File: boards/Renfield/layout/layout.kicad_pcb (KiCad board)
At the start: 4 copper layers, 74 x 52 mm, 99 parts, among them IC1 DS04-254-1-04BK-SMT, IC2 TPD4E05U06QDQARQ1, J1 2060-452/998-404, J2 61000821121, J3 ?, J4 61000418221, J5 USB4105-GF-A, Q1 CSD13380F3, Q2 CSD17318Q2, SW1 B3U-1000P, SW2 B3U-1000P, U1 TPSM33606S5QRDNRQ1, U2 TPS259482LYWPR, U3 TPS74501PDRVR, U4 STM32G0B1KEU6N, U5 TCPP01-M12

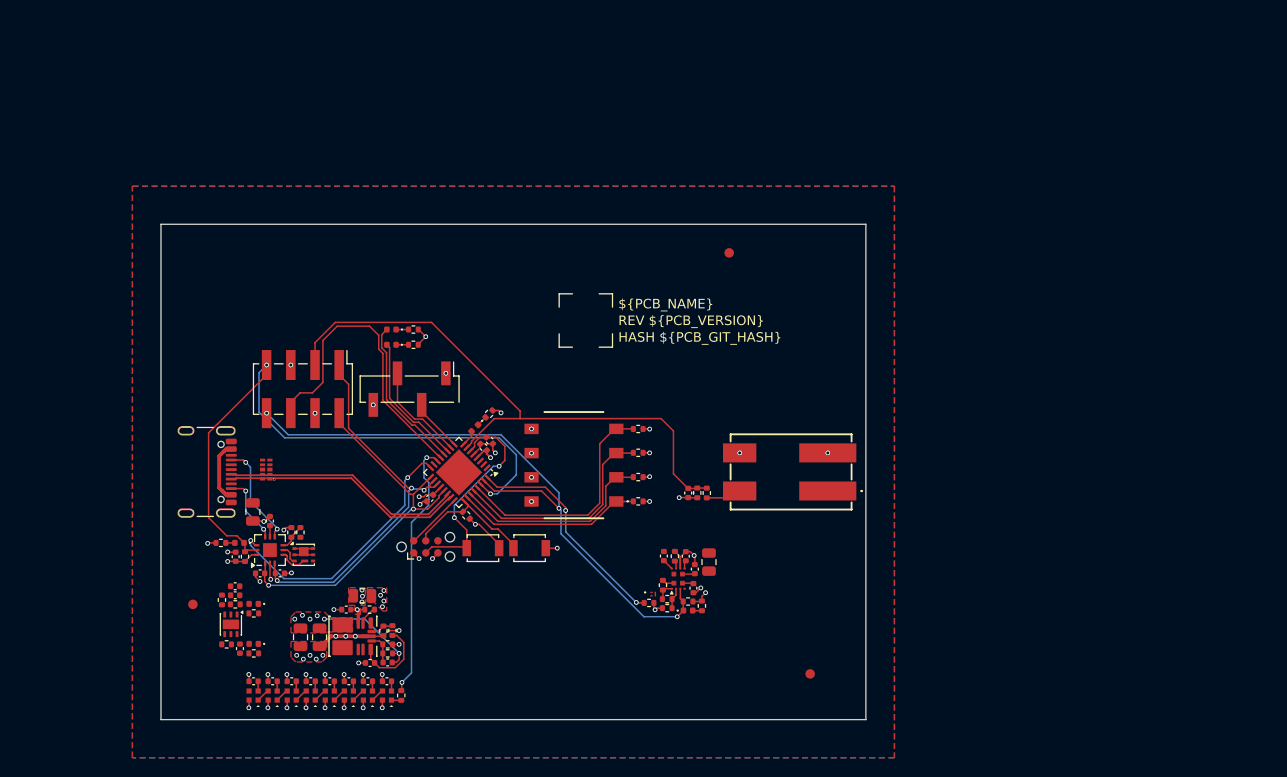
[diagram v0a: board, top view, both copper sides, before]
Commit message: refactor(Renfield): strip to minimal PD sink dev board
Simplified Renfield down to the essentials needed for STM32G0B1 UCPD
firmware development. Roughly halves the BOM and resolves a real
bootstrap bug in the rail topology.

Architectural fix: buck now sits on VBUS_RAW, not VBUS_PROT.
  Before: VBUS_RAW \u2192 FET \u2192 VBUS_PROT \u2192 Buck \u2192 V3V3 \u2192 TCPP01 VCC
          \u2191 but FET needs VCC to close (DS12900 conditions all VGS
          specs on VCC = 3.0\u20133.6 V). Circular; board couldn't boot.
  After:  VBUS_RAW \u2500\u252c\u2500\u2500 Buck \u2192 V3V3 \u2192 MCU + TCPP01 VCC
                  \u2514\u2500\u2500 FET  \u2192 VBUS_PROT \u2192 WAGO
          MCU boots off the receptacle directly; FET gates only the
          LOAD rail. MCU survives OVP trips. Matches DS12900 \u00a76.1:
          "separate the low voltage MCU domain from the high-voltage
          power path."

Removed (dev-board features not needed for PD firmware work):
  - TPS259482L eFuse + CSD13380F3 disable shunt + SPLYGD LED +
    VBUS_OUT bulk + VBUS_OUT ADC divider
  - 8x IN-PI15 WS2812 V-bargraph + series R
  - 4-pos DIP switch + 4x pull-up resistors
  - BOOT0 + RESET tactile buttons
  - 2x4 PD-dev probe header + 1x4 UART header
  - TPD4E05U06 USB-data ESD array
  - TPS74501P LDO (buck now goes VBUS_RAW \u2192 3.3 V directly with
    the TPSM33606S3 fixed-trim variant)
  - 5 V rail (nothing consumed it)
  - 5V_RAIL LED, EFUSE_NOT_GOOD LED

Kept (everything firmware dev actually needs):
  - USB-C 16P receptacle + TCPP01-M12 + CSD17318Q2 gated FET
  - TPSM33606S3 buck \u2192 V3V3
  - STM32G0B1KEU6N with UCPD1 / USB FS / SWD / UART
  - WAGO 2060-452 load output (post-FET)
  - Tag-Connect SWD pads
  - 5 status LEDs: 3V3_RAIL, TCPP01_FLT, heartbeat, PD contract, USB enum
  - 12x round \u00d81.0 mm SMD test pads (VBUS_RAW, VBUS_PROT, FET_GATE,
    V3V3, UART_TX, UART_RX, CC1, CC2, SCOPE_MARKER, TCPP01_FLT, 2x GND)

Other cleanup:
  - Dropped C_VBUS_RAW \u2014 TCPP01 internal C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
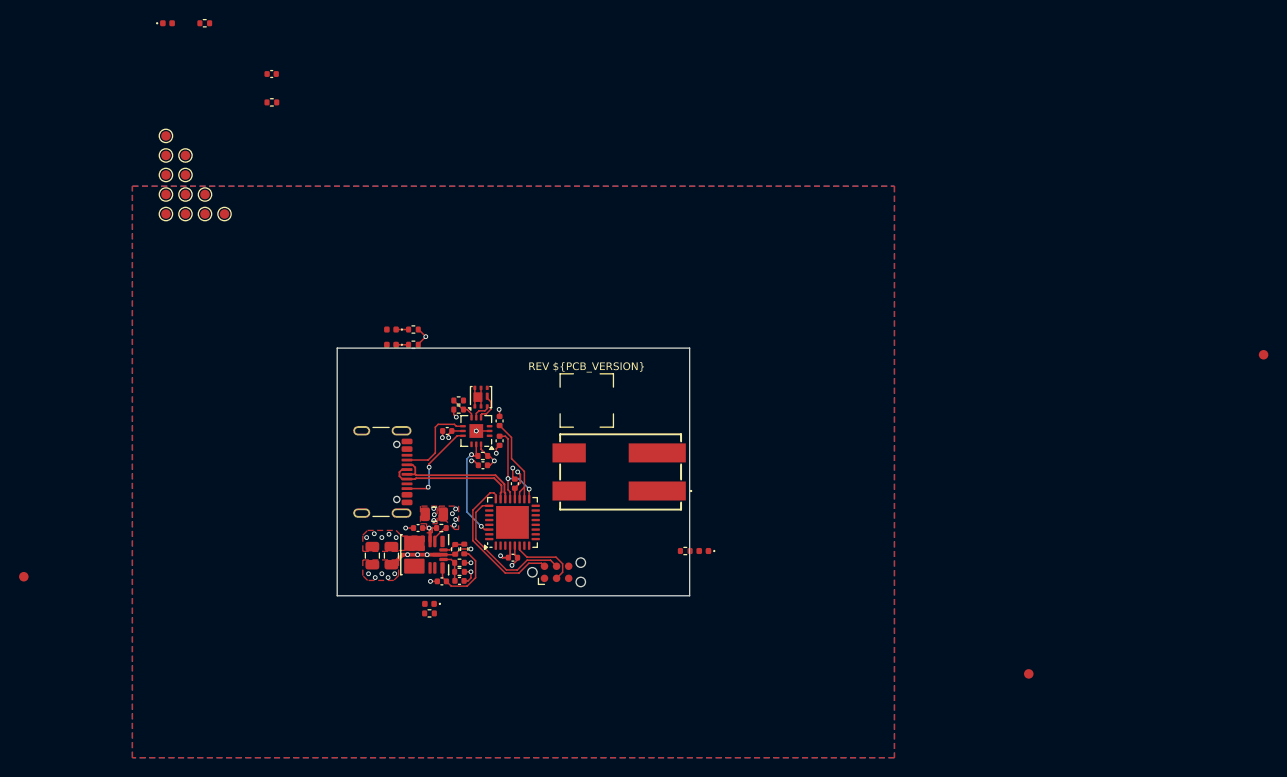
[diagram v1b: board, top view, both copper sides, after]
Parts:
- removed the C12 at (126.7, 122.0)
- removed the C13 at (124.7, 122.0)
- removed C14, C20, C26, C27, C28, C29: GRM155Z71A105KE01D, kicad_libraries_kicad-footprints_Capacitor_SMD@9.0.3:C_0402_1005Metric
- removed C15: GCM1555C1H100FA16D, kicad_libraries_kicad-footprints_Capacitor_SMD@9.0.3:C_0402_1005Metric
- removed C16: GRM21BZ71H475KE15K, kicad_libraries_kicad-footprints_Capacitor_SMD@9.0.3:C_0805_2012Metric
- removed C17, C22, C24: GCM155R71H104KE02D, kicad_libraries_kicad-footprints_Capacitor_SMD@9.0.3:C_0402_1005Metric
- removed C18, C19: GRM21BZ71A226ME15K, kicad_libraries_kicad-footprints_Capacitor_SMD@9.0.3:C_0805_2012Metric
- removed C21: GCM1555C1H102FA16D, kicad_libraries_kicad-footprints_Capacitor_SMD@9.0.3:C_0402_1005Metric
- removed C23, C25: GRM1555CYA103GE01D, kicad_libraries_kicad-footprints_Capacitor_SMD@9.0.3:C_0402_1005Metric
- removed D10, D6, D7, D8, D9: IN-PI15TAT5R5G5B, diodeinc_registry_components_Inolux_IN-PI15TAT5R5G5B@0.1.1:IN-PI15TAT5R5G5B
- removed D11: VLMS1500-GS08, kicad_libraries_kicad-footprints_LED_SMD@9.0.3:LED_0402_1005Metric
- removed D12: LTST-C281KSKT, kicad_libraries_kicad-footprints_LED_SMD@9.0.3:LED_0402_1005Metric
- removed the D3 at (136.7, 123.5)
- removed the D4 at (134.7, 123.5)
- removed the D5 at (132.7, 123.5)
- removed IC1: DS04-254-1-04BK-SMT, diodeinc_registry_components_DS04-254-1-04BK-SMT@0.3.7:DS04254104BKSMT
- removed IC2: TPD4E05U06QDQARQ1, diodeinc_registry_components_TPD4E05U06QDQARQ1@0.4.5:DQA_R-PUSON-N10_
- removed the J2 at (127.9, 91.3)
- removed J4: 61000418221, kicad_libraries_kicad-footprints_Connector_PinHeader_2.54mm@9.0.3:PinHeader_1x04_P2.54mm_Vertical_SMD_Pin1Left
- removed the Q1 at (164.7, 112.8)
- removed the R12 at (168.3, 113.6)
- removed R15: ERJ-2RKF9092X, kicad_libraries_kicad-footprints_Resistor_SMD@9.0.3:R_0402_1005Metric
- removed R16, R19: ERJ-2RKF1002X, kicad_libraries_kicad-footprints_Resistor_SMD@9.0.3:R_0402_1005Metric
- removed R17: ERJ-2RKF4700X, kicad_libraries_kicad-footprints_Resistor_SMD@9.0.3:R_0402_1005Metric
- removed R18, R21, R22, R27: ERJ-2RKF1003X, kicad_libraries_kicad-footprints_Resistor_SMD@9.0.3:R_0402_1005Metric
- removed R20: ERJ-2GE0R00X, kicad_libraries_kicad-footprints_Resistor_SMD@9.0.3:R_0402_1005Metric
- removed R23: ERJ-2RKF3653X, kicad_libraries_kicad-footprints_Resistor_SMD@9.0.3:R_0402_1005Metric
- removed R24: ERJ-2RKF2672X, kicad_libraries_kicad-footprints_Resistor_SMD@9.0.3:R_0402_1005Metric
- removed R25: ERJ-2RKF1053X, kicad_libraries_kicad-footprints_Resistor_SMD@9.0.3:R_0402_1005Metric
- removed R26: ERJ-2RKF8060X, kicad_libraries_kicad-footprints_Resistor_SMD@9.0.3:R_0402_1005Metric
- removed R28: ERJ-2RKF5102X, kicad_libraries_kicad-footprints_Resistor_SMD@9.0.3:R_0402_1005Metric
- removed R29: ERJ-2RKF2553X, kicad_libraries_kicad-footprints_Resistor_SMD@9.0.3:R_0402_1005Metric
- removed the R4 at (163.1, 103.1)
- removed the R5 at (163.1, 100.5)
- removed the R6 at (163.1, 98.0)
- removed SW1, SW2: B3U-1000P, diodeinc_registry_components_B3U-1000P@0.2.1:B3U-1000P
- removed the U3 at (120.3, 116.0)
- removed U4: STM32G0B1KEU6N, diodeinc_registry_components_STMicroelectronics_STM32G0B1KxUxN@0.1.4:QFN-32-1EP_5x5mm_P0.5mm_EP3.45x3.45mm
- added R11: ERJ-2RKF1003X, kicad_libraries_kicad-footprints_Resistor_SMD@9.0.3:R_0402_1005Metric, F.Cu at (144.8, 108.1)
- added TP1: ?, kicad_libraries_kicad-footprints_TestPoint@9.0.3:TestPoint_Pad_D1.0mm, F.Cu at (113.5, 72.9)
- added TP10: ?, kicad_libraries_kicad-footprints_TestPoint@9.0.3:TestPoint_Pad_D1.0mm, F.Cu at (119.7, 72.9)
- added TP11: ?, kicad_libraries_kicad-footprints_TestPoint@9.0.3:TestPoint_Pad_D1.0mm, F.Cu at (113.5, 64.7)
- added TP12: ?, kicad_libraries_kicad-footprints_TestPoint@9.0.3:TestPoint_Pad_D1.0mm, F.Cu at (115.6, 66.8)
- added TP2: ?, kicad_libraries_kicad-footprints_TestPoint@9.0.3:TestPoint_Pad_D1.0mm, F.Cu at (113.5, 70.9)
- added TP3: ?, kicad_libraries_kicad-footprints_TestPoint@9.0.3:TestPoint_Pad_D1.0mm, F.Cu at (115.6, 72.9)
- added TP4: ?, kicad_libraries_kicad-footprints_TestPoint@9.0.3:TestPoint_Pad_D1.0mm, F.Cu at (113.5, 68.8)
- added TP5: ?, kicad_libraries_kicad-footprints_TestPoint@9.0.3:TestPoint_Pad_D1.0mm, F.Cu at (115.6, 70.9)
- added TP6: ?, kicad_libraries_kicad-footprints_TestPoint@9.0.3:TestPoint_Pad_D1.0mm, F.Cu at (117.6, 72.9)
- added TP7: ?, kicad_libraries_kicad-footprints_TestPoint@9.0.3:TestPoint_Pad_D1.0mm, F.Cu at (113.5, 66.8)
- added TP8: ?, kicad_libraries_kicad-footprints_TestPoint@9.0.3:TestPoint_Pad_D1.0mm, F.Cu at (115.6, 68.8)
- added TP9: ?, kicad_libraries_kicad-footprints_TestPoint@9.0.3:TestPoint_Pad_D1.0mm, F.Cu at (117.6, 70.9)
- C4: value GRM21BZ71H475KE15K -> GCM1555C1H100FA16D; footprint kicad_libraries_kicad-footprints_Capacitor_SMD@9.0.3:C_0805_2012Metric -> kicad_libraries_kicad-footprints_Capacitor_SMD@9.0.3:C_0402_1005Metric
- C6: value GRM1555CYA103GE01D -> GCM155R71H104KE02D
- C7, C8: value GRM155Z71A105KE01D -> GRM21BZ71A226ME15K; footprint kicad_libraries_kicad-footprints_Capacitor_SMD@9.0.3:C_0402_1005Metric -> kicad_libraries_kicad-footprints_Capacitor_SMD@9.0.3:C_0805_2012Metric
- D2: value VLMG1500-GS08 -> LTST-C281KSKT
- R10: value ERJ-2RKF8200X -> ERJ-2RKF1003X
- R2: value ERJ-2RKF1501X -> ERJ-2RKF1002X
- R3: value ERJ-2RKF1002X -> ERJ-2RKF8200X
- R8: value ERJ-2RKF1003X -> ERJ-2RKF1002X
- R9: value ERJ-2RKF4700X -> ERJ-2GE0R00X
- U1: value TPSM33606S5QRDNRQ1 -> TPSM33606S3QRDNRQ1
- U2: value TPS259482LYWPR -> STM32G0B1KEU6N; footprint diodeinc_registry_components_Texas_Instruments_TPS259482@0.1.3:TPS259482 -> diodeinc_registry_components_STMicroelectronics_STM32G0B1KxUxN@0.1.4:QFN-32-1EP_5x5mm_P0.5mm_EP3.45x3.45mm
- moved D2 65.8 mm to (113.7, 52.9), turned to 0 degrees
- moved R3 58.5 mm to (117.6, 52.9), turned to 0 degrees
- moved R2 57.9 mm to (124.6, 61.2), turned to 0 degrees
- moved FID1 57.1 mm to (228.7, 87.7)
- moved D4 48.8 mm to (170.0, 108.3)
- moved R5 48.8 mm to (168.0, 108.3)
- moved C3 44.8 mm to (124.6, 58.2), turned to 0 degrees
- moved C11 29.8 mm to (150.1, 101.2), turned to 90 degrees
- moved C2 28.7 mm to (148.6, 96.7), turned to -90 degrees
- moved C6 28.6 mm to (140.0, 105.9), turned to 180 degrees
- moved C1 28.1 mm to (148.6, 94.7), turned to 90 degrees
- moved C13 27.7 mm to (146.8, 99.3), turned to 180 degrees
- moved R12 27.1 mm to (146.8, 98.3), turned to 0 degrees
- moved C4 26.3 mm to (144.3, 111.4), turned to 180 degrees
- moved R9 25.7 mm to (144.3, 110.5), turned to 180 degrees
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- renumbered C30 to C12, C31 to C13, D13 to D3, D14 to D4, D15 to D5, J3 to J2, J5 to J3, Q2 to Q1, R30 to R12, R31 to R13, R32 to R14, R11 to R4, R13 to R5, R14 to R6, U5 to U3
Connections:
- C10 pad 1: V5V -> V3V3
- C11 pad 1: V5V -> V3V3
- C4 pad 1: VBUS_OUT -> V3V3
- C4 pad 2: GND -> U_BUCK.FB
- C6 pad 1: ADC_VBUS_OUT -> VBUS_RAW
- C7 pad 1: V5V -> V3V3
- C8 pad 1: V5V -> V3V3
- C9 pad 1: V5V -> U_BUCK.VCC
- D2 pad 1: LED_5V_RAIL_K -> LED_HEARTBEAT_K
- D2 pad 2: V5V -> HEARTBEAT_LED
- J1 pad 1: VBUS_OUT -> VBUS_PROT
- R10 pad 1: LED_HEARTBEAT_K -> U_BUCK.MODE_SYNC
- R2 pad 1: LED_5V_RAIL_K -> SWD_SWCLK
- R3 pad 1: SWD_SWCLK -> LED_HEARTBEAT_K
- R7 pad 1: DIP_SW4 -> VBUS_RAW
- R7 pad 2: V3V3 -> U_BUCK.EN
- R8 pad 1: EFUSE_DISABLE -> U_BUCK.FB
- R9 pad 2: LED_EFUSE_NOT_GOOD_A -> U_BUCK.FB
- U1 pad 3: VBUS_PROT -> VBUS_RAW
- U1 pad 4: V5V -> V3V3
- U2 pad 1: EFUSE_EN -> U_MCU.PB9
- U2 pad 10: U_EFUSE.ITIMER -> UART_RX
- U2 pad 11: VBUS_OUT -> PD_CONTRACT_LED
- U2 pad 12: VBUS_PROT -> USB_ENUM_LED
- U2 pad 2: U_EFUSE.OVLO -> U_MCU.PC14
- U2 pad 3: EFUSE_SPLY_GOOD_N -> U_MCU.PC15
- U2 pad 4: U_EFUSE.RCBCTRL -> V3V3
- U2 pad 5: VBUS_PROT -> GND
- U2 pad 6: VBUS_OUT -> NRST
- U2 pad 7: U_EFUSE.DVDT -> U_MCU.PA0
- U2 pad 8: GND -> HEARTBEAT_LED
- U2 pad 9: EFUSE_IMON -> UART_TX
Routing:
- net EFUSE_SPLY_GOOD_N: track 66.8 -> 0.00 mm, vias 3 -> 0
- net ADC_VBUS_OUT: track 61.6 -> 0.00 mm
- net TCPP01_FLT: track 66.9 -> 11.4 mm
- net SCOPE_MARKER: track 32.2 -> 0.00 mm
- net GND: track 54.8 -> 22.9 mm, vias 57 -> 25
- net CC1_MCU: track 41.5 -> 10.3 mm, vias 3 -> 0
- net CC2_MCU: track 41.2 -> 11.2 mm
- net TCPP01_DB: track 28.4 -> 0.00 mm, vias 2 -> 0
- net WS2812_DATA: track 27.3 -> 0.00 mm, vias 2 -> 0
- net DIP_SW4: track 25.0 -> 0.00 mm
- net EFUSE_DISABLE: track 23.5 -> 0.00 mm, vias 2 -> 0
- net DIP_SW3: track 23.3 -> 0.00 mm
- net DIP_SW2: track 21.4 -> 0.00 mm
- net V5V: track 19.7 -> 0.00 mm, vias 6 -> 0
- net DIP_SW1: track 19.6 -> 0.00 mm
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- added copper zone on F.Cu, net V3V3
- added copper zone on F.Cu, net VBUS_RAW
- removed copper zone on F.Cu, net V5V
- removed copper zone on F.Cu, net VBUS_PROT
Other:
- board size 74 x 52 mm -> 37 x 26 mm

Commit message: layout(Renfield): finalize pinout for routing + swap buck to TPS709 LDO
Pinout tweaks for easier layout:
- TCPP01 FLT\u2192PA9, DB\u2192PA10 (reclaimed DBCC pins, short routes to TCPP01)
- Status LEDs moved to PB0/PB1/PA7 (closer to LED cluster)
- SCOPE_MARKER moved to PD0 (TIM16_CH1, frees PA6)
- CC1/CC2 swapped on TCPP01\u2192MCU side (saves a trace crossing)
- DBCC1/DBCC2 dropped; firmware releases G0 internal Rd via
  SYSCFG_CFGR1.UCPD1_STROBE before driving TCPP01 DB high

Rail:
- Replace TPSM33606S3 buck with TPS70933 LDO (150 mA, 30 V Vin,
  ~1 \u00b5A Iq). At ~10 mA MCU+TCPP01 load, ~170 mW worst-case dissipation
  at 20 V is fine for the 2\u00d72 mm WSON. EN floats (internal pull-up).

Test pads:
- Dropped VBUS_RAW, VBUS_PROT, V3V3, FET_GATE, TCPP01_FLT, one GND.
- Added TP_OVP_SENSE (TCPP01 divider tap, ~VBUS/17) as safe proxy
  for VBUS probe.
- CC1/CC2 pads moved to connector-side for raw BMC capture.

Misc cleanup:
- Bump Wago 2060-4xx_998-404 to 0.1.1.
- Drop TPSM336xx-Q1 vendor bundle.

Build: 40 components, US \.01 @ qty 20.
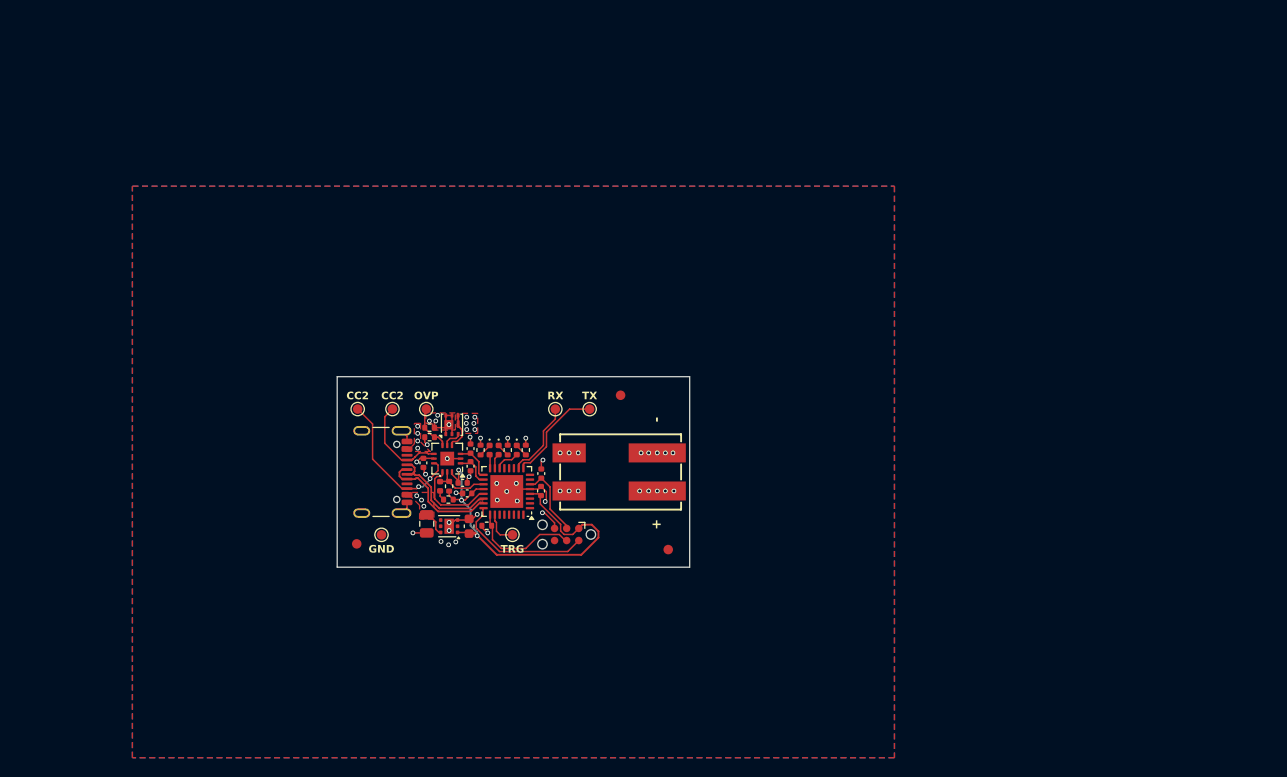
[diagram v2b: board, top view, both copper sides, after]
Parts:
- removed the C6 at (140.0, 105.9)
- removed the C7 at (135.2, 108.8)
- removed the C8 at (137.2, 108.8)
- removed the C9 at (142.5, 111.5)
- removed the D1 at (141.2, 113.8)
- removed D5: VLMB1500-GS08, kicad_libraries_kicad-footprints_LED_SMD@9.0.3:LED_0402_1005Metric
- removed the R1 at (141.2, 114.8)
- removed R10, R11: ERJ-2RKF1003X, kicad_libraries_kicad-footprints_Resistor_SMD@9.0.3:R_0402_1005Metric
- removed the R7 at (142.4, 105.9)
- removed the R8 at (144.3, 109.5)
- removed R9: ERJ-2GE0R00X, kicad_libraries_kicad-footprints_Resistor_SMD@9.0.3:R_0402_1005Metric
- removed TP10, TP11, TP12: ?, kicad_libraries_kicad-footprints_TestPoint@9.0.3:TestPoint_Pad_D1.0mm
- removed the TP5 at (115.6, 70.9)
- removed the TP7 at (113.5, 66.8)
- added D4: VLMB1500-GS08, kicad_libraries_kicad-footprints_LED_SMD@9.0.3:LED_0402_1005Metric, F.Cu at (150.3, 97.7)
- C4: value GCM1555C1H100FA16D -> GRM21BZ71H475KE15K; footprint kicad_libraries_kicad-footprints_Capacitor_SMD@9.0.3:C_0402_1005Metric -> kicad_libraries_kicad-footprints_Capacitor_SMD@9.0.3:C_0805_2012Metric
- C5: value GRM21BZ71H475KE15K -> GRM188Z71C475KE21D; footprint kicad_libraries_kicad-footprints_Capacitor_SMD@9.0.3:C_0805_2012Metric -> kicad_libraries_kicad-footprints_Capacitor_SMD@9.0.3:C_0603_1608Metric
- J1: footprint diodeinc_registry_components_Wago_2060-4xx_998-404@0.1.0:2060-4xx_998-404-2P-white -> diodeinc_registry_components_Wago_2060-4xx_998-404@0.1.1:2060-4xx_998-404-2P-white
- U1: value TPSM33606S3QRDNRQ1 -> TPS70933QDRVRQ1; footprint diodeinc_registry_components_Texas_Instruments_TPSM336xx-Q1@0.1.0:TPSM336xx-Q1 -> diodeinc_registry_components_Texas_Instruments_TPS709-Q1@0.1.0:TPS709-Q1
- U2: value STM32G0B1KEU6N -> STM32G0B1KBU6N
- V1: moved to B.Cu
- moved FID1 67.6 mm to (161.2, 92.0)
- moved D1 56.7 mm to (148.4, 97.7), turned to -90 degrees
- moved R2 54.9 mm to (149.4, 97.7), turned to 90 degrees
- moved C3 50.6 mm to (152.9, 100.2), turned to 90 degrees
- moved R1 49.8 mm to (147.2, 105.7), turned to 180 degrees
- moved TP5 46.6 mm to (149.9, 106.6)
- moved TP7 46.2 mm to (158.0, 93.4)
- moved TP6 46.0 mm to (154.4, 93.4)
- moved FID2 40.0 mm to (166.2, 108.2)
- moved TP3 39.5 mm to (136.2, 106.6)
- moved TP4 36.8 mm to (140.8, 93.4)
- moved FID3 35.1 mm to (133.6, 107.5)
- moved TP1 31.4 mm to (137.3, 93.4)
- moved TP2 30.2 mm to (133.7, 93.4)
- moved D3 28.5 mm to (142.3, 101.5), turned to -90 degrees
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- renumbered C10 to C6, C11 to C7, C12 to C8, C13 to C9, D2 to D1, D3 to D2, D4 to D3, R2 to R1, R3 to R2, R4 to R3, R5 to R4, R6 to R5, R12 to R6, R13 to R7, R14 to R8, TP6 to TP5, TP8 to TP6, TP9 to TP7
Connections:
- C4 pad 1: V3V3 -> VBUS_RAW
- C4 pad 2: U_BUCK.FB -> GND
- C5 pad 1: VBUS_RAW -> V3V3
- R7 pad 1: VBUS_OVP_SENSE -> OVP_SENSE
- R8 pad 2: VBUS_OVP_SENSE -> OVP_SENSE
- TP1 pad 1: CC1_MCU -> USB_C_CC1
- TP2 pad 1: CC2_MCU -> USB_C_CC2
- TP3 pad 1: FET_GATE -> GND
- TP4 pad 1: GND -> OVP_SENSE
- U1 pad 1: U_BUCK.PGOOD -> V3V3
- U1 pad 2: U_BUCK.EN -> unconnected-(U_LDO.U1:2)
- U1 pad 3: VBUS_RAW -> GND
- U1 pad 4: V3V3 -> U_LDO.EN
- U1 pad 6: unconnected-(U_BUCK.U1:6) -> VBUS_RAW
- U1 pad 7: U_BUCK.NC_U1_BOOT -> GND
- U2 pad 11: PD_CONTRACT_LED -> U_MCU.PA4
- U2 pad 12: USB_ENUM_LED -> U_MCU.PA5
- U2 pad 13: SCOPE_MARKER -> U_MCU.PA6
- U2 pad 14: U_MCU.PA7 -> USB_ENUM_LED
- U2 pad 15: U_MCU.PB0 -> HEARTBEAT_LED
- U2 pad 16: TCPP01_DB -> PD_CONTRACT_LED
- U2 pad 17: CC2_MCU -> CC1_MCU
- U2 pad 18: CC1_MCU -> CC2_MCU
- U2 pad 19: CC1_MCU -> TCPP01_FLT
- U2 pad 21: CC2_MCU -> TCPP01_DB
- U2 pad 26: U_MCU.PD0 -> SCOPE_MARKER
- U2 pad 30: TCPP01_FLT -> U_MCU.PB6
- U2 pad 8: HEARTBEAT_LED -> U_MCU.PA1
- U3 pad 6: VBUS_OVP_SENSE -> OVP_SENSE
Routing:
- net V3V3: track 11.0 -> 43.1 mm, vias 9 -> 3
- net UART_TX: track 0.00 -> 10.7 mm
- net TCPP01_DB: track 0.00 -> 9.30 mm
- net U_BUCK.VCC: track 8.48 -> 0.00 mm
- net UART_RX: track 0.00 -> 8.17 mm
- net CC2_MCU: track 11.2 -> 3.83 mm, vias 2 -> 0
- net USB_C_CC2: track 9.55 -> 16.0 mm
- net CC1_MCU: track 10.3 -> 4.13 mm
- net TCPP01_FLT: track 11.4 -> 6.15 mm, vias 2 -> 0
- net OVP_SENSE: track 0.00 -> 4.91 mm
- net SCOPE_MARKER: track 0.00 -> 3.64 mm
- net SWD_SWCLK: track 15.0 -> 11.8 mm
- net U_BUCK.FB: track 3.23 -> 0.00 mm
- net GND: track 22.9 -> 25.9 mm, vias 25 -> 33
- net VBUS_OVP_SENSE: track 2.84 -> 0.00 mm
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- added copper zone on F.Cu, net VBUS_PROT
- added copper zone on In2.Cu, net VBUS_PROT
- added copper zone on In2.Cu, net VBUS_RAW
- removed copper zone on F.Cu, net V3V3
- removed copper zone on In2.Cu, net V3V3
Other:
- board size 37 x 26 mm -> 37 x 20 mm
- board text added: "+"
- board text added: "-"
- board text added: "CC2"
- board text added: "GND"
- board text added: "OVP"
- board text added: "RX"
- board text added: "TRG"
- board text added: "TX"
